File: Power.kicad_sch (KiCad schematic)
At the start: 28 parts, among them J1 12V, J11 Conn_01x02_Pin, J14 Conn_01x02_Pin, J15 Conn_01x02_Pin, U1 TPS7A2633DRVR, U2 TPS54202DDC

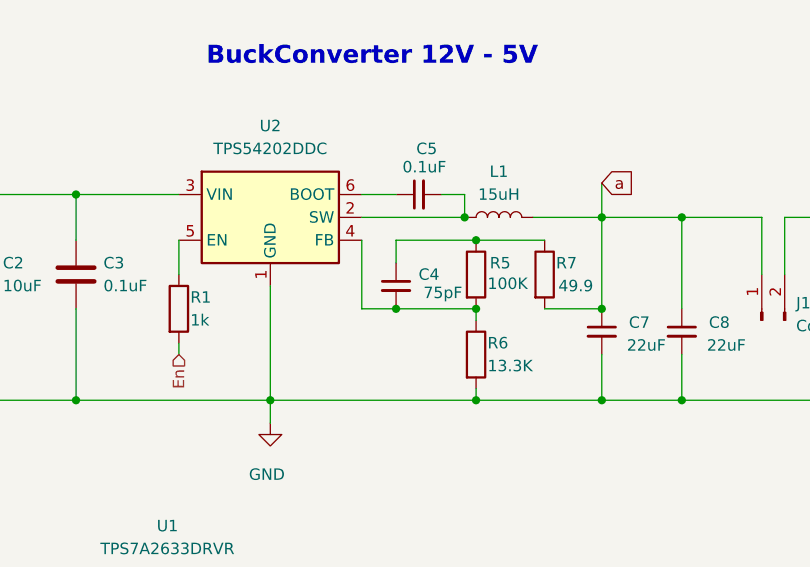
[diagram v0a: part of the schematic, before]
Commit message: Update antenna
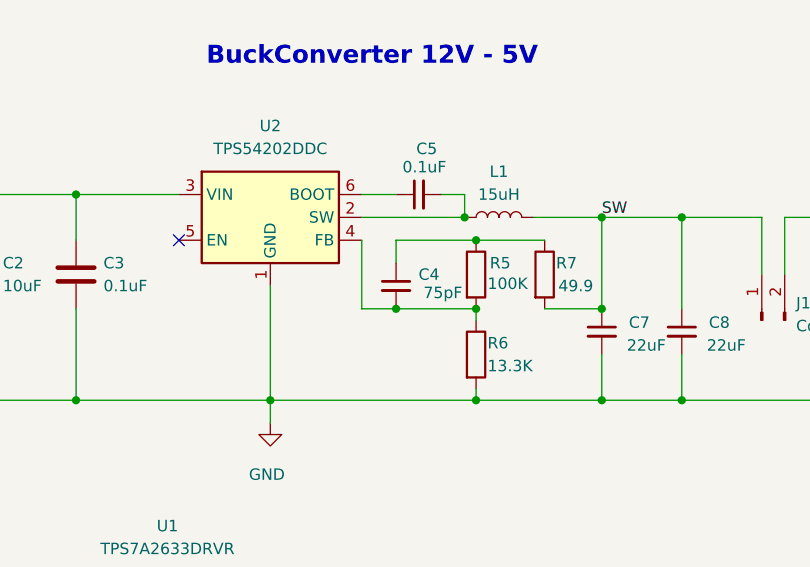
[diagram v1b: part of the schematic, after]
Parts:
- removed R1: 1k, Resistor_SMD:R_0402_1005Metric, symbol Device:R
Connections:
- net a renamed SW
- no-connect marks 0 -> 1
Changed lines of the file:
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@@
 		(color 0 0 0 0)
 	)
+	(no_connect
+		(at 132.08 71.12)
+	)
 	(wire
 		(pts
@@
 	(wire
 		(pts
-			(xy 132.08 74.93) (xy 132.08 71.12)
-		)
-		(stroke
-			(width 0)
-			(type default)
-		)
-	)
-	(wire
-		(pts
 			(xy 184.15 115.57) (xy 184.15 110.49)
 		)
@@
 	(wire
 		(pts
-			(xy 132.08 83.82) (xy 132.08 82.55)
-		)
-		(stroke
-			(width 0)
-			(type default)
-		)
-	)
-	(wire
-		(pts
 			(xy 161.29 66.04) (xy 163.83 66.04)
 		)
@@
 		(pts
 			(xy 152.4 78.74) (xy 156.21 78.74)
-		)
-		(stroke
-			(width 0)
-			(type default)
-		)
-	)
-	(wire
-		(pts
-			(xy 179.07 64.77) (xy 179.07 68.58)
 		)
 		(stroke
@@
 		)
 	)
-	(global_label "a"
-		(shape input)
-		(at 179.07 64.77 0)
+	(label "SW"
+		(at 179.07 68.58 0)
 		(fields_autoplaced yes)
 		(effects
@@
 				(size 1.27 1.27)
 			)
-			(justify left)
-		)
-		(property "Intersheetrefs" "${INTERSHEET_REFS}"
-			(at 183.2042 64.77 0)
-			(effects
-				(font
-					(size 1.27 1.27)
-				)
-				(justify left)
-				(hide yes)
-			)
-		)
-	)
-	(hierarchical_label "En"
-		(shape input)
-		(at 132.08 83.82 270)
-		(fields_autoplaced yes)
-		(effects
-			(font
-				(size 1.27 1.27)
-			)
-			(justify right)
+			(justify left bottom)
 		)
 	)
@@
 					(unit 1)
 				)
-			)
-		)
-	)
-	(symbol
-		(lib_id "Device:R")
-		(at 132.08 78.74 0)
-		(unit 1)
-		(exclude_from_sim no)
-		(in_bom yes)
-		(on_board yes)
-		(dnp no)
-		(property "Reference" "R1"
-			(at 133.35 77.47 0)
-			(effects
-				(font
-					(size 1.27 1.27)
-				)
-				(justify left)
-			)
-		)
-		(property "Value" "1k"
-			(at 133.35 80.01 0)
-			(effects
-				(font
-					(size 1.27 1.27)
-				)
-				(justify left)
-			)
-		)
-		(property "Footprint" "Resistor_SMD:R_0402_1005Metric"
-			(at 130.302 78.74 90)
-			(effects
-				(font
-					(size 1.27 1.27)
-				)
-				(hide yes)
-			)
-		)
-		(property "Datasheet" "~"
-			(at 132.08 78.74 0)
-			(effects
-				(font
-					(size 1.27 1.27)
-				)
-				(hide yes)
-			)
-		)
-		(property "Description" "Resistor"
-			(at 132.08 78.74 0)
-			(effects
-				(font
-					(size 1.27 1.27)
-				)
-				(hide yes)
-			)
-		)
-		(property "MANUFACTURER" ""
-			(at 132.08 78.74 0)
-			(effects
-				(font
-					(size 1.27 1.27)
-				)
-				(hide yes)
-			)
-		)
-		(property "MAXIMUM_PACKAGE_HEIGHT" ""
-			(at 132.08 78.74 0)
-			(effects
-				(font
-					(size 1.27 1.27)
-				)
-				(hide yes)
-			)
-		)
-		(property "PARTREV" ""
-			(at 132.08 78.74 0)
-			(effects
-				(font
-					(size 1.27 1.27)
-				)
-				(hide yes)
-			)
-		)
-		(property "STANDARD" ""
-			(at 132.08 78.74 0)
-			(effects
-				(font
-					(size 1.27 1.27)
-				)
-				(hide yes)
-			)
-		)
-		(property "Sim.Device" ""
-			(at 132.08 78.74 0)
-			(effects
-				(font
-					(size 1.27 1.27)
-				)
-				(hide yes)
-			)
-		)
-		(property "Sim.Pins" ""
-			(at 132.08 78.74 0)
-			(effects
-				(font
-					(size 1.27 1.27)
-				)
-				(hide yes)
-			)
-		)
-		(property "Sim.Type" ""
-			(at 132.08 78.74 0)
-			(effects
-				(font
-					(size 1.27 1.27)
-				)
-				(hide yes)
-			)
-		)
-		(pin "1"
-		)
-		(pin "2"
-		)
-		(instances
-			(project "airlora-kicad"
-				(path "/59d971df-d6c1-4ef7-a085-bf08b7b16047/be77b740-d58b-414b-97ce-61f1d1685314/af8bb3f5-67b6-4471-83fd-9297b14489a9"
-					(reference "R1")
-					(unit 1)
-				)
